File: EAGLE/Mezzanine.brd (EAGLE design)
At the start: 80 x 72.4 mm, 11 parts

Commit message: error checks done
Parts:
- R1, R2, R3: value (none) -> 50
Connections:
- net GND: now also U$13.P$2, U$13.P$3, U$14.P$2, U$14.P$3, U$15.P$2, U$15.P$3, U$16.P$2, U$16.P$3
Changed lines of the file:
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@@
 <grid distance="5" unitdist="mm" unit="mm" style="lines" multiple="1" display="yes" altdistance="0.01" altunitdist="mm" altunit="mm"/>
 <layers>
-<layer number="1" name="Top" color="4" fill="1" visible="no" active="yes"/>
+<layer number="1" name="Top" color="4" fill="1" visible="yes" active="yes"/>
 <layer number="2" name="Route2" color="16" fill="1" visible="no" active="no"/>
 <layer number="3" name="Route3" color="17" fill="1" visible="no" active="no"/>
@@
 <element name="U$10" library="Mini-Circuits-QBA-07+_Phase-shifter" package="QBA-07+" value="QBA-07+" x="49.9" y="62" smashed="yes"/>
 <element name="U$11" library="Mini-Circuits-QBA-07+_Phase-shifter" package="QBA-07+" value="QBA-07+" x="49.9" y="37.8" smashed="yes" rot="R180"/>
-<element name="R1" library="oresat-rcl" package=".0402-A-NOSILK" value="" x="78.85" y="68.35" smashed="yes" rot="R270">
+<element name="R1" library="oresat-rcl" package=".0402-A-NOSILK" value="50" x="78.85" y="68.35" smashed="yes" rot="R270">
 <attribute name="NAME" x="79.5" y="69.25" size="0.5" layer="25" font="vector" ratio="15" rot="R270"/>
 <attribute name="NAME" x="78.85" y="68.35" size="0.2" layer="33" ratio="15" rot="R270" align="center"/>
 <attribute name="VALUE" x="77.45" y="69.25" size="0.8" layer="27" font="vector" ratio="15" rot="R270"/>
 </element>
-<element name="R2" library="oresat-rcl" package=".0402-A-NOSILK" value="" x="56" y="59" smashed="yes" rot="R180">
+<element name="R2" library="oresat-rcl" package=".0402-A-NOSILK" value="50" x="56" y="59" smashed="yes" rot="R180">
 <attribute name="NAME" x="56.9" y="58.35" size="0.5" layer="25" font="vector" ratio="15" rot="R180"/>
 <attribute name="NAME" x="56" y="59" size="0.2" layer="33" ratio="15" rot="R180" align="center"/>
 <attribute name="VALUE" x="56.9" y="60.4" size="0.8" layer="27" font="vector" ratio="15" rot="R180"/>
 </element>
-<element name="R3" library="oresat-rcl" package=".0402-A-NOSILK" value="" x="44.33" y="40.8" smashed="yes">
+<element name="R3" library="oresat-rcl" package=".0402-A-NOSILK" value="50" x="44.33" y="40.8" smashed="yes">
 <attribute name="NAME" x="43.43" y="41.45" size="0.5" layer="25" font="vector" ratio="15"/>
 <attribute name="NAME" x="44.33" y="40.8" size="0.2" layer="33" ratio="15" align="center"/>
@@
 <contactref element="U$12" pad="P$2"/>
 <contactref element="U$12" pad="P$3"/>
+<contactref element="U$13" pad="P$2"/>
+<contactref element="U$13" pad="P$3"/>
+<contactref element="U$14" pad="P$2"/>
+<contactref element="U$14" pad="P$3"/>
+<contactref element="U$15" pad="P$2"/>
+<contactref element="U$15" pad="P$3"/>
+<contactref element="U$16" pad="P$2"/>
+<contactref element="U$16" pad="P$3"/>
 <wire x1="82.425" y1="77" x2="85.375" y2="77" width="0" layer="19" extent="1-1"/>
-<wire x1="80.08" y1="64.985" x2="82.425" y2="77" width="0" layer="19" extent="1-1"/>
+<wire x1="78.85" y1="68.9" x2="82.425" y2="77" width="0" layer="19" extent="1-1"/>
+<wire x1="80.08" y1="64.985" x2="78.85" y2="68.9" width="0" layer="19" extent="1-1"/>
 <wire x1="81.35" y1="64.985" x2="80.08" y2="64.985" width="0" layer="19" extent="1-1"/>
 <wire x1="82.62" y1="64.985" x2="81.35" y2="64.985" width="0" layer="19" extent="1-1"/>
 <wire x1="81.35" y1="62" x2="81.35" y2="64.985" width="0" layer="19" extent="1-1"/>
 <wire x1="81.35" y1="59.015" x2="81.35" y2="62" width="0" layer="19" extent="1-1"/>
+<wire x1="82.62" y1="59.015" x2="81.35" y2="59.015" width="0" layer="19" extent="1-1"/>
 <wire x1="80.08" y1="59.015" x2="81.35" y2="59.015" width="0" layer="19" extent="1-1"/>
-<wire x1="82.62" y1="59.015" x2="81.35" y2="59.015" width="0" layer="19" extent="1-1"/>
-<wire x1="51.17" y1="59.015" x2="80.08" y2="59.015" width="0" layer="19" extent="1-1"/>
+<wire x1="67.84298125" y1="65.757015625" x2="78.85" y2="68.9" width="0" layer="19" extent="1-1"/>
+<wire x1="65.757015625" y1="67.84298125" x2="67.84298125" y2="65.757015625" width="0" layer="19" extent="1-1"/>
+<wire x1="56.55" y1="59" x2="65.757015625" y2="67.84298125" width="0" layer="19" extent="1-1"/>
+<wire x1="51.17" y1="59.015" x2="56.55" y2="59" width="0" layer="19" extent="1-1"/>
 <wire x1="49.9" y1="59.015" x2="51.17" y2="59.015" width="0" layer="19" extent="1-1"/>
 <wire x1="48.63" y1="59.015" x2="49.9" y2="59.015" width="0" layer="19" extent="1-1"/>
@@
 <wire x1="51.17" y1="64.985" x2="49.9" y2="64.985" width="0" layer="19" extent="1-1"/>
 <wire x1="48.63" y1="64.985" x2="49.9" y2="64.985" width="0" layer="19" extent="1-1"/>
-<wire x1="51.17" y1="40.785" x2="82.62" y2="59.015" width="0" layer="19" extent="1-1"/>
+<wire x1="34.04298125" y1="67.84298125" x2="48.63" y2="64.985" width="0" layer="19" extent="1-1"/>
+<wire x1="31.957015625" y1="65.757015625" x2="34.04298125" y2="67.84298125" width="0" layer="19" extent="1-1"/>
+<wire x1="51.17" y1="40.785" x2="51.17" y2="59.015" width="0" layer="19" extent="1-1"/>
 <wire x1="49.9" y1="40.785" x2="51.17" y2="40.785" width="0" layer="19" extent="1-1"/>
 <wire x1="48.63" y1="40.785" x2="49.9" y2="40.785" width="0" layer="19" extent="1-1"/>
@@
 <wire x1="51.17" y1="34.815" x2="49.9" y2="34.815" width="0" layer="19" extent="1-1"/>
 <wire x1="48.63" y1="34.815" x2="49.9" y2="34.815" width="0" layer="19" extent="1-1"/>
-<wire x1="56.55" y1="59" x2="85.375" y2="77" width="0" layer="19" extent="1-1"/>
-<wire x1="78.85" y1="68.9" x2="56.55" y2="59" width="0" layer="19" extent="1-1"/>
-<wire x1="43.78" y1="40.8" x2="78.85" y2="68.9" width="0" layer="19" extent="1-1"/>
+<wire x1="43.78" y1="40.8" x2="48.63" y2="40.785" width="0" layer="19" extent="1-1"/>
+<wire x1="34.04298125" y1="31.957015625" x2="43.78" y2="40.8" width="0" layer="19" extent="1-1"/>
+<wire x1="31.957015625" y1="34.04298125" x2="34.04298125" y2="31.957015625" width="0" layer="19" extent="1-1"/>
+<wire x1="65.757015625" y1="31.957015625" x2="51.17" y2="34.815" width="0" layer="19" extent="1-1"/>
+<wire x1="67.84298125" y1="34.04298125" x2="65.757015625" y2="31.957015625" width="0" layer="19" extent="1-1"/>
 </signal>
 <signal name="N$1">

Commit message: TestBoard ready for design review and order
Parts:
- R1, R2, R3: device oresat-rcl:.0402-A-NOSILK -> oresat-rcl:.0805-B-NOSILK
- moved R1 0.65 mm to (78.8, 69.0)
- moved R2 0.65 mm to (56.6, 59.0)
- moved R3 0.34 mm to (44.0, 40.8)
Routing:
- added copper zone on layer 1, net GND
- added copper zone on layer 15, net GND
- added copper zone on layer 16, net GND
- added copper zone on layer 2, net GND

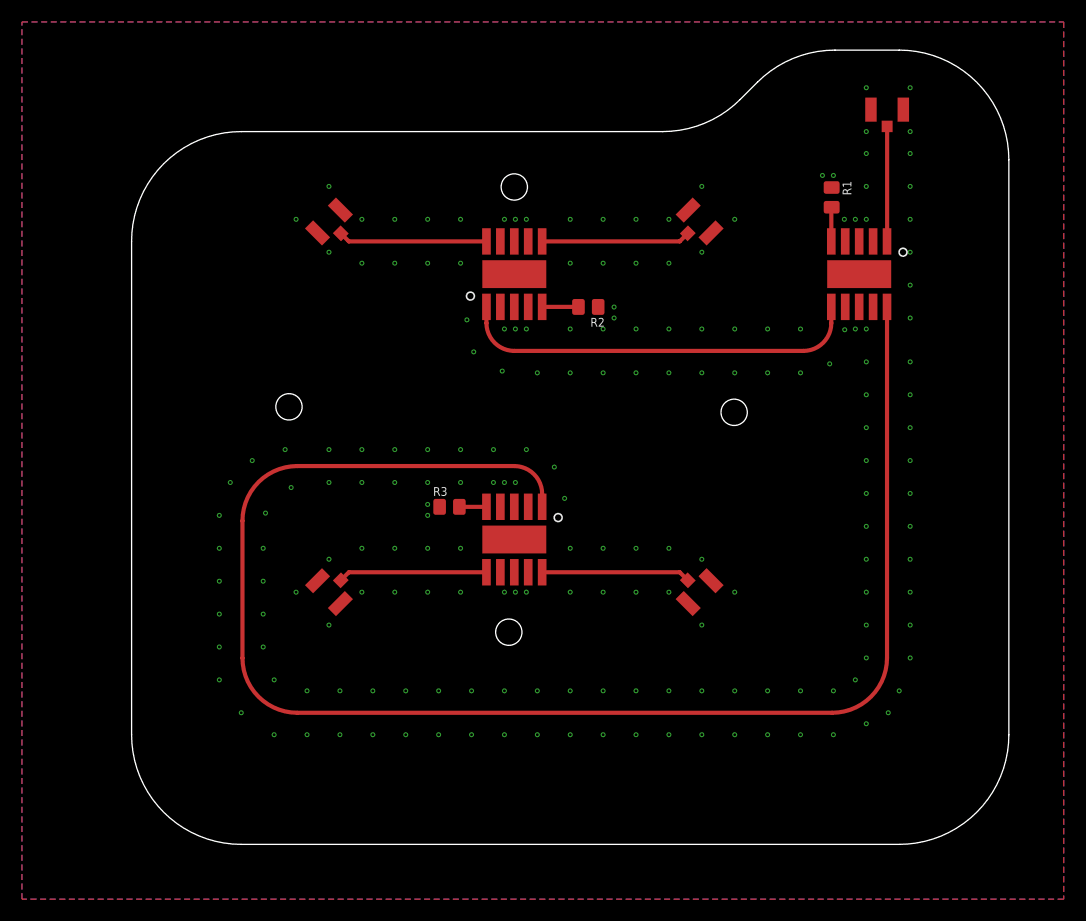
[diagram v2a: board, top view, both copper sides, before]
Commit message: rerouted mezzanine
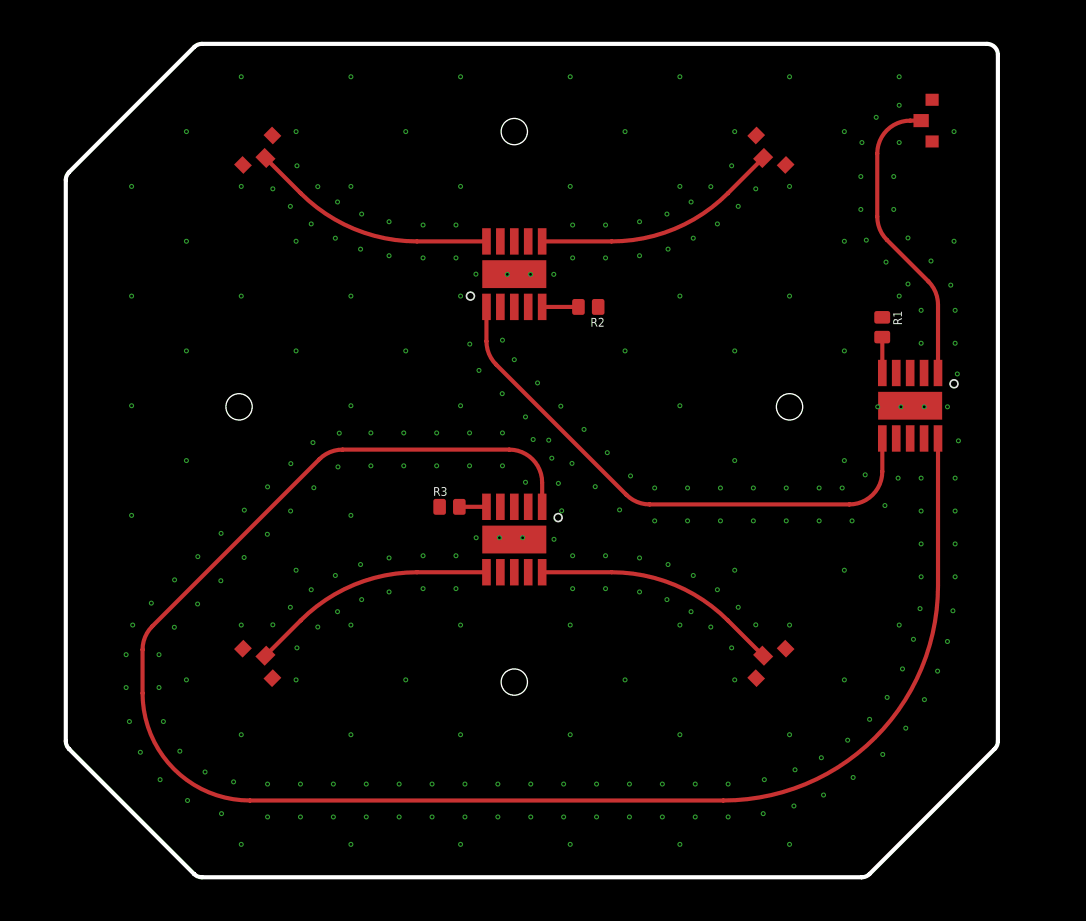
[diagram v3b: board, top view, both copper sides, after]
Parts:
- removed U$12, U$13, U$14, U$15, U$16: U.FL-R-SMA, J-HRS-U.FL-R-SMT-1(10)-M-RF:U.FL-R-SMT
- added U$1, U$2, U$3, U$4, U$5: R107064070, J-Radiall-R107064070-RF:R107064070
- moved U$9 12.9 mm to (86.0, 50.0)
- moved R1 12.7 mm to (83.5, 57.2)
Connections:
- net GND: now also U$1.P$2, U$1.P$3, U$2.P$2, U$2.P$3, U$3.P$2, U$3.P$3, U$4.P$2, U$4.P$3, U$5.P$2, U$5.P$3; no longer U$12.P$2, U$12.P$3, U$13.P$2, U$13.P$3, U$14.P$2, U$14.P$3, U$15.P$2, U$15.P$3, U$16.P$2, U$16.P$3
- net N$1: now also U$1.P$1; no longer U$12.P$1
- net UHF_0: now also U$2.P$1; no longer U$13.P$1
- net UHF_180: now also U$4.P$1; no longer U$15.P$1
- net UHF_270: now also U$5.P$1; no longer U$16.P$1
- net UHF_90: now also U$3.P$1; no longer U$14.P$1
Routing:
- net N$1: track 10.5 -> 27.2 mm
- net N$2: track 36.5 -> 50.0 mm
- net N$5: track 139.1 -> 149.9 mm
- net UHF_180: track 13.6 -> 22.4 mm
- net UHF_270: track 13.6 -> 22.4 mm
- net UHF_90: track 13.6 -> 22.4 mm
- net UHF_0: track 13.6 -> 22.4 mm
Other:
- board size 80 x 72.4 mm -> 85 x 76 mm

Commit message: Minor additions to Eric's board: Brought in edges to make it slightly smaller because money and it doesn't need to be big, and added appropriate fasteners, including shoulder bolts in the X axis for precision alignment, and regular M2 bolts in the Y axis. Added STOP and RESTRICT layers to keep out solder mask and grounds from fasteners.
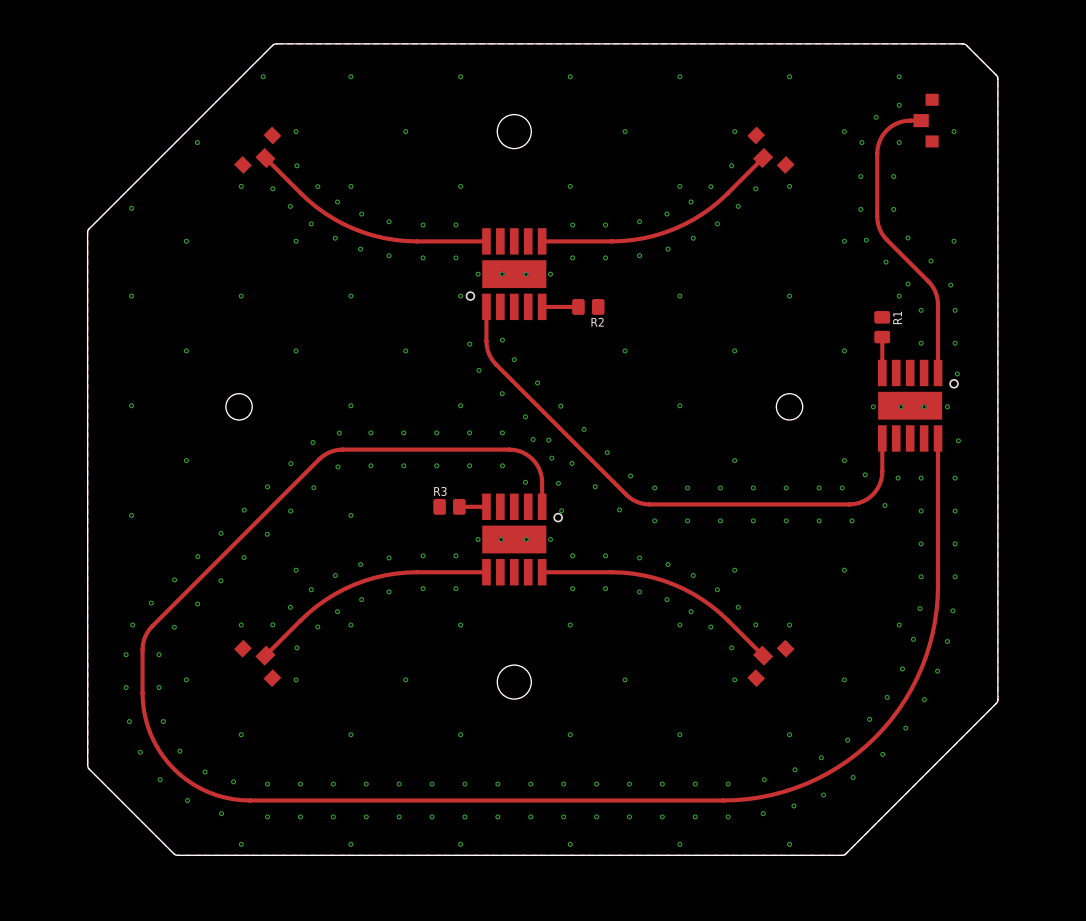
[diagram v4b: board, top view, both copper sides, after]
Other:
- board size 85 x 76 mm -> 83 x 74 mm
